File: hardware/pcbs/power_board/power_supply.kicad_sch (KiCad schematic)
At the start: 25 parts, among them J13 Barrel Jack, J14 ScrewTerminal_02, U13 LMR38020, U14 LMR38020

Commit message: boards: fix minor bom issues
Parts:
- C26, C27, C28, C29: Shop https://store.comet.bg/Catalogue/Product/24725/ -> https://store.comet.bg/Catalogue/Product/16789/
- R50: Shop https://eu.mouser.com/ProductDetail/Bourns/CR1206-FX-3162EL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 -> https://eu.mouser.com/ProductDetail/Bourns/CR0805-FX-3162EL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
- R51: Shop https://eu.mouser.com/ProductDetail/Bourns/CR0603-FX-1372EL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 -> https://eu.mouser.com/ProductDetail/Bourns/CR0805-FX-1372EL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
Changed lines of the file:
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@@
 			)
 		)
-		(property "Shop" "https://store.comet.bg/Catalogue/Product/24725/"
+		(property "Shop" "https://store.comet.bg/Catalogue/Product/16789/"
 			(at 128.27 133.35 0)
 			(effects
@@
 			)
 		)
-		(property "Shop" "https://eu.mouser.com/ProductDetail/Bourns/CR1206-FX-3162ELF?qs=sGAEpiMZZMvdGkrng054t%252BRNGJdg958R4Syzj%252BoTzfo%3D"
+		(property "Shop" "https://eu.mouser.com/ProductDetail/Bourns/CR0805-FX-3162ELF?qs=4vGXhLEMbUxw0LpIaWR6Eg%3D%3D"
 			(at 187.96 128.27 0)
 			(effects
@@
 			)
 		)
-		(property "Shop" "https://store.comet.bg/Catalogue/Product/24725/"
+		(property "Shop" "https://store.comet.bg/Catalogue/Product/16789/"
 			(at 172.72 74.93 0)
 			(effects
@@
 			)
 		)
-		(property "Shop" "https://store.comet.bg/Catalogue/Product/24725/"
+		(property "Shop" "https://store.comet.bg/Catalogue/Product/16789/"
 			(at 128.27 92.71 0)
 			(effects
@@
 			)
 		)
-		(property "Shop" "https://store.comet.bg/Catalogue/Product/24725/"
+		(property "Shop" "https://store.comet.bg/Catalogue/Product/16789/"
 			(at 172.72 115.57 0)
 			(effects
@@
 			)
 		)
-		(property "Shop" "https://eu.mouser.com/ProductDetail/Bourns/CR0603-FX-1372ELF?qs=sGAEpiMZZMvdGkrng054t%2Fh5BnJxeWSz2MQjIqgi9jc%3D"
+		(property "Shop" "https://eu.mouser.com/ProductDetail/Bourns/CR0805-FX-1372ELF?qs=Hqdsf0hGw%2FCg%2FaUiKya1YA%3D%3D"
 			(at 187.96 138.43 0)
 			(effects

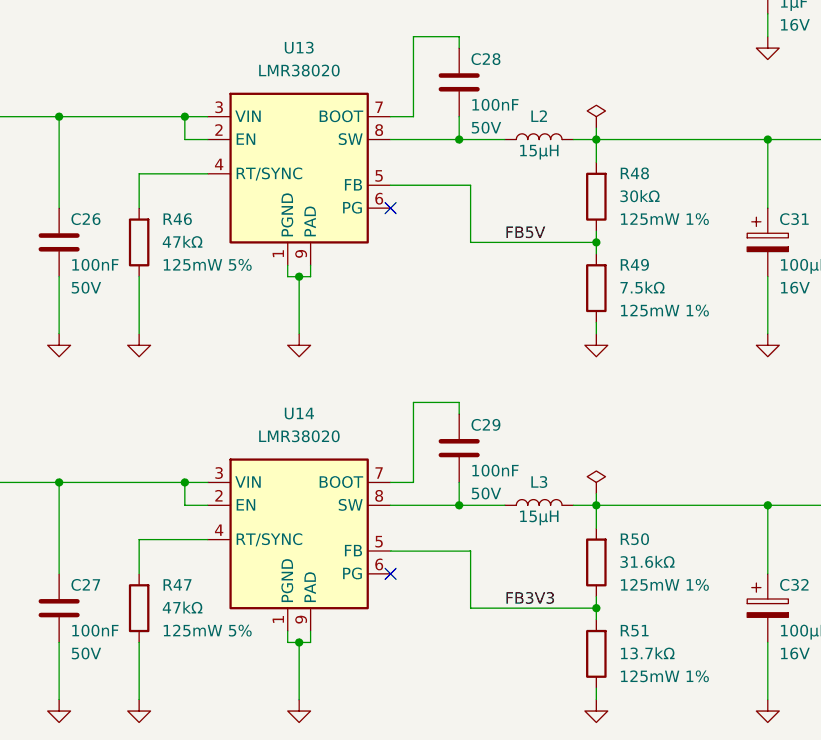
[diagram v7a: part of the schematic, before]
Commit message: power_board: proper enable circuit for meanwell power modules
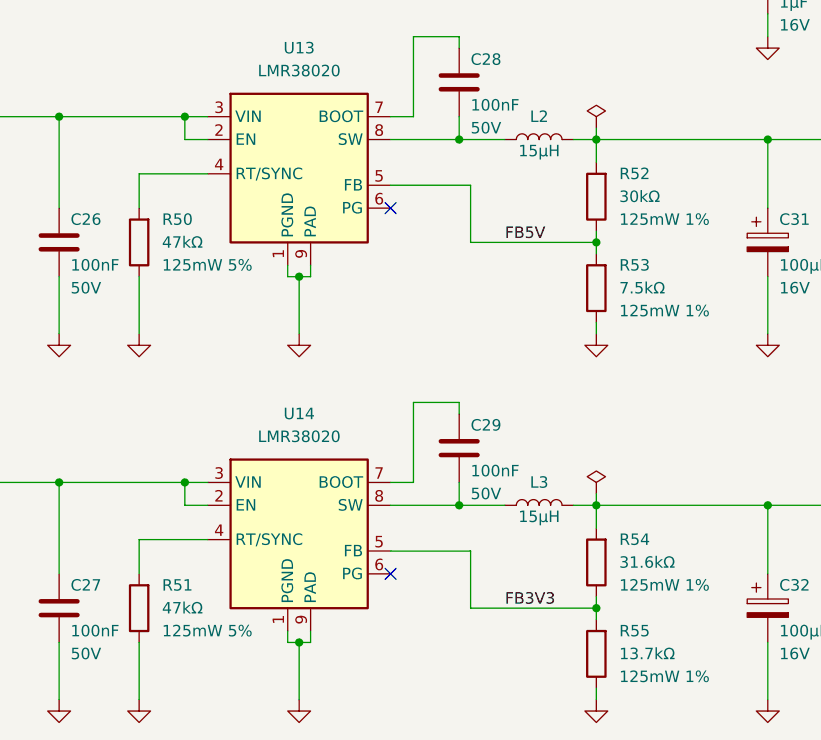
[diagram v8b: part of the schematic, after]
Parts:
- renumbered R46 to R50, R47 to R51, R48 to R52, R49 to R53, R50 to R54, R51 to R55
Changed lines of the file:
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@@
 		(on_board yes)
 		(dnp no)
-		(property "Reference" "R50"
+		(property "Reference" "R54"
 			(at 190.5 125.73 0)
 			(effects
@@
 			(project "power_board"
 				(path "/4b166175-80a4-48c6-994d-6e62a6160b87/61c6854b-d478-45fd-8007-466db156e311"
-					(reference "R50")
+					(reference "R54")
 					(unit 1)
 				)
@@
 		(on_board yes)
 		(dnp no)
-		(property "Reference" "R49"
+		(property "Reference" "R53"
 			(at 190.5 95.25 0)
 			(effects
@@
 			(project "power_board"
 				(path "/4b166175-80a4-48c6-994d-6e62a6160b87/61c6854b-d478-45fd-8007-466db156e311"
-					(reference "R49")
+					(reference "R53")
 					(unit 1)
 				)
@@
 		(on_board yes)
 		(dnp no)
-		(property "Reference" "R51"
+		(property "Reference" "R55"
 			(at 190.5 135.89 0)
 			(effects
@@
 			(project "power_board"
 				(path "/4b166175-80a4-48c6-994d-6e62a6160b87/61c6854b-d478-45fd-8007-466db156e311"
-					(reference "R51")
+					(reference "R55")
 					(unit 1)
 				)
@@
 		(on_board yes)
 		(dnp no)
-		(property "Reference" "R46"
+		(property "Reference" "R50"
 			(at 139.7 90.17 0)
 			(effects
@@
 			(project "power_board"
 				(path "/4b166175-80a4-48c6-994d-6e62a6160b87/61c6854b-d478-45fd-8007-466db156e311"
-					(reference "R46")
+					(reference "R50")
 					(unit 1)
 				)
@@
 		(on_board yes)
 		(dnp no)
-		(property "Reference" "R48"
+		(property "Reference" "R52"
 			(at 190.5 85.09 0)
 			(effects
@@
 			(project "power_board"
 				(path "/4b166175-80a4-48c6-994d-6e62a6160b87/61c6854b-d478-45fd-8007-466db156e311"
-					(reference "R48")
+					(reference "R52")
 					(unit 1)
 				)
@@
 		(on_board yes)
 		(dnp no)
-		(property "Reference" "R47"
+		(property "Reference" "R51"
 			(at 139.7 130.81 0)
 			(effects
@@
 			(project "power_board"
 				(path "/4b166175-80a4-48c6-994d-6e62a6160b87/61c6854b-d478-45fd-8007-466db156e311"
-					(reference "R47")
-					(unit 1)
-				)
+					(reference "R51")
+					(unit 1)
+				)
